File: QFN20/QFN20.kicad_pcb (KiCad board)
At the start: 2 copper layers, 12.2 x 25.7 mm, 10 parts, among them J1 Conn_01x10, J2 Conn_02x10_Counter_Clockwise, J3 Conn_01x10, J4 Conn_02x10_Counter_Clockwise

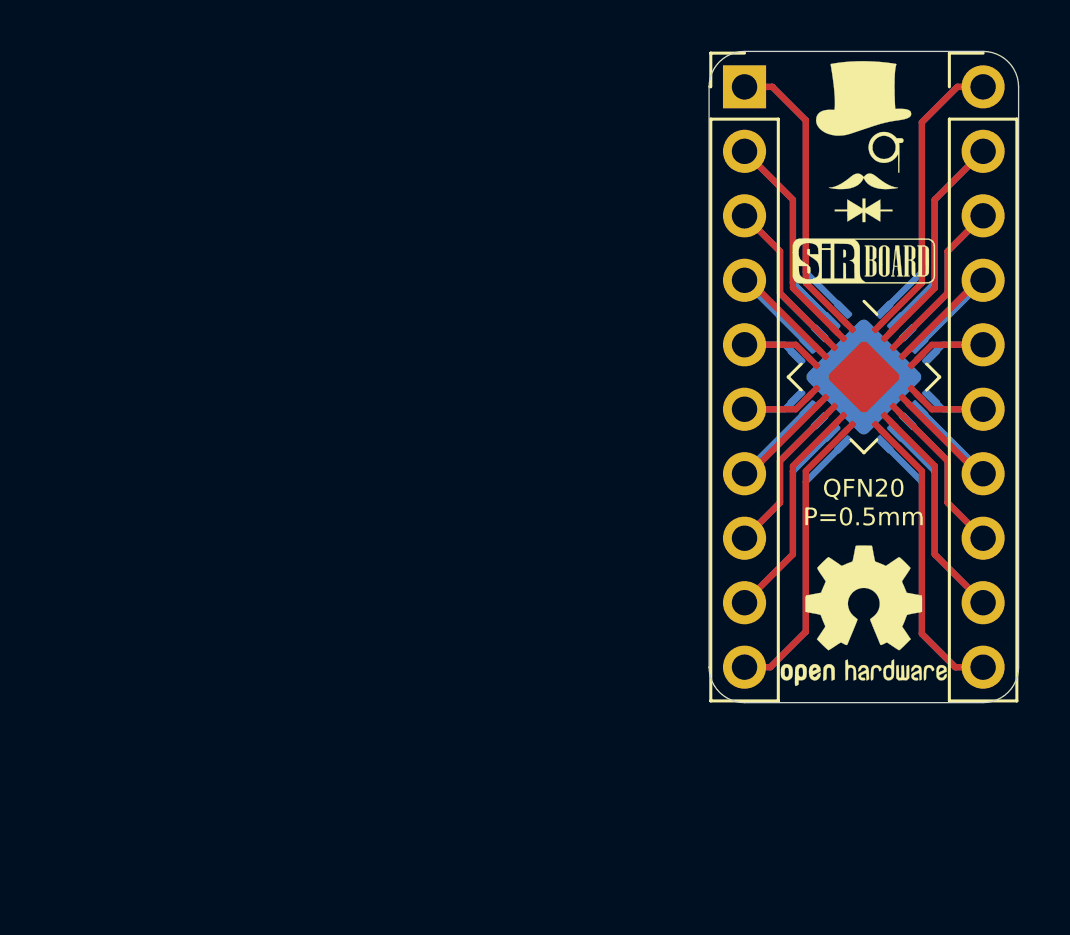
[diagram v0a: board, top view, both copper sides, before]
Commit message: Silkscreens and sizes updated
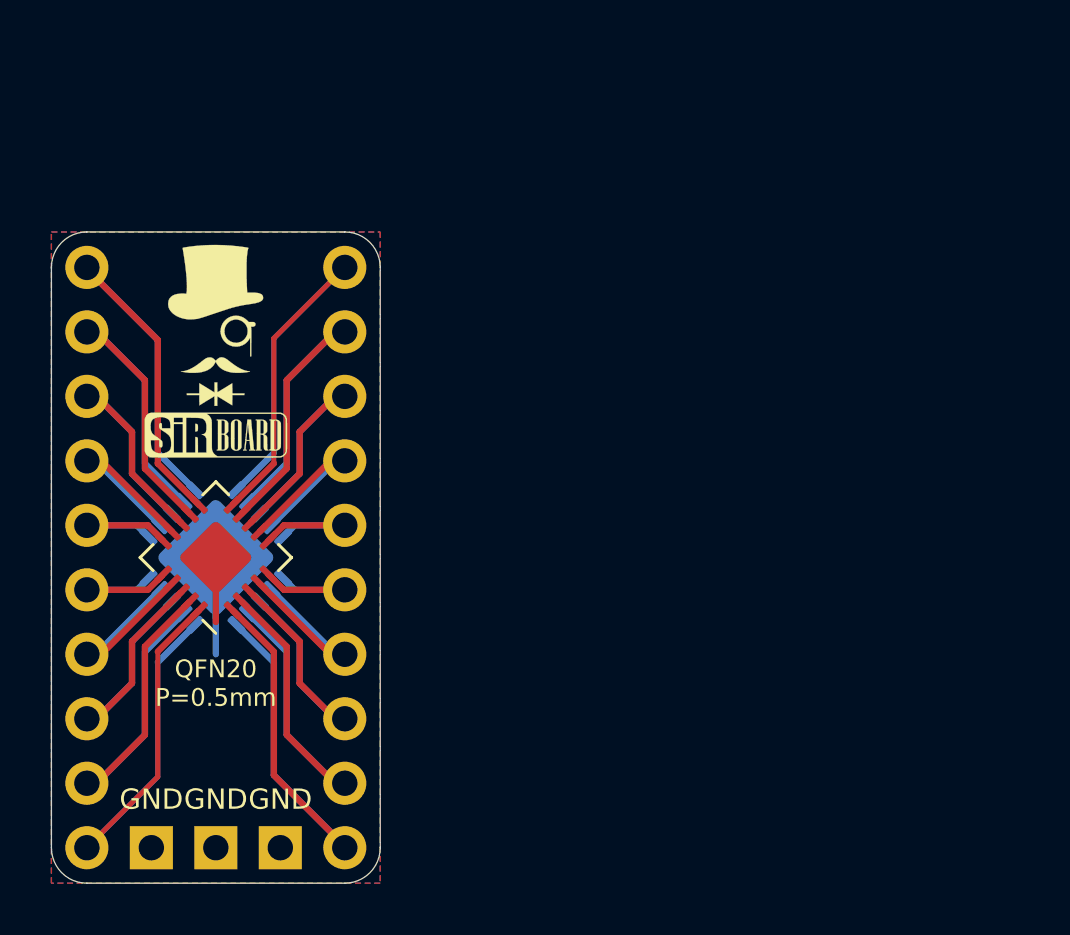
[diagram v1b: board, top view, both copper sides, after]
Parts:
- removed REF** (x2): OSHW-Logo2_7.3x6mm_SilkScreen, Symbol:OSHW-Logo2_7.3x6mm_SilkScreen
- added J5: Conn_01x03, Connector_PinHeader_2.54mm:PinHeader_1x03_P2.54mm_Vertical, F.Cu at (99.3, 70.6)
- moved J3 46.3 mm to (91.7, 70.6), turned to 180 degrees
- moved J1 33.9 mm to (101.9, 70.6), turned to 180 degrees
- moved G*** 27.9 mm to (96.9, 49.9), turned to 180 degrees
- moved G*** 26.5 mm to (96.8, 50.0)
- moved J2 26.5 mm to (96.8, 59.2), turned to 135 degrees
- moved J4 26.5 mm to (96.8, 59.2), turned to 225 degrees
- moved G*** 26.4 mm to (96.8, 54.4)
- moved G*** 25.7 mm to (96.8, 54.4), turned to 180 degrees
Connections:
- J2 pad 21: (no net) -> Net-(J5-Pad1)
- J4 pad 21: (no net) -> Net-(J5-Pad1)
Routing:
- net Net-(J5-Pad1): track 0.00 -> 8.72 mm
- net Net-(J2-Pad11): track 22.7 -> 21.4 mm
- net Net-(J1-Pad1): track 22.7 -> 21.7 mm
- net Net-(J2-Pad20): track 22.6 -> 21.7 mm
- net Net-(J1-Pad10): track 22.6 -> 21.7 mm
- added copper zone on B.Cu, net Net-(J5-Pad1)
- added copper zone on F.Cu, net Net-(J5-Pad1)
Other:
- board size 12.2 x 25.7 mm -> 13 x 25.7 mm
- board text added: "GND"

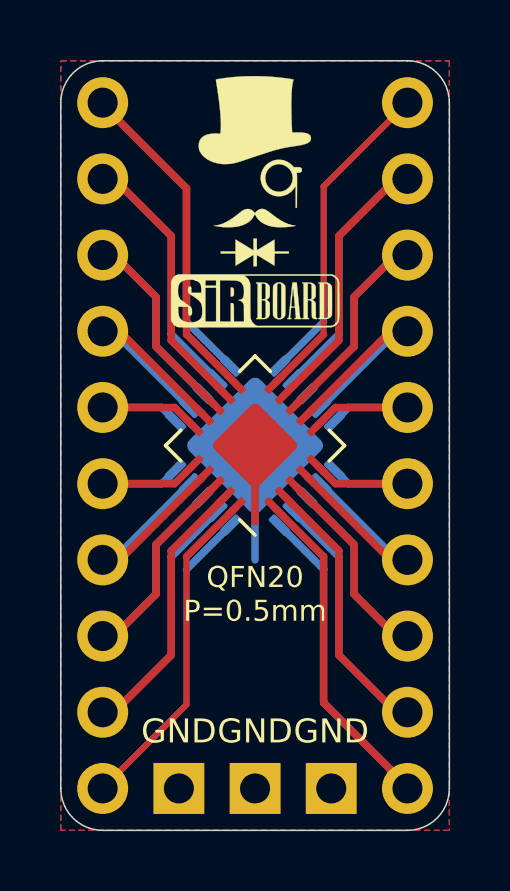
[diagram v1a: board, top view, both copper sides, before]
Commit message: Dimensions Added And TQFP64 Added
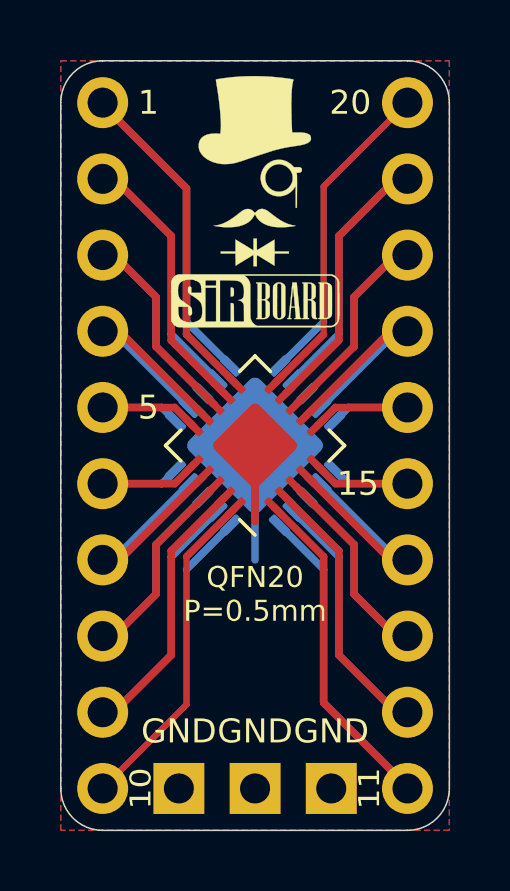
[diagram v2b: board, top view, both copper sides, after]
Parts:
- J1, J3: moved to B.Cu
- turned J1 to 0 degrees
- turned J3 to 0 degrees
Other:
- board text added: "1"
- board text added: "10"
- board text added: "11"
- board text added: "15"
- board text added: "20"
- board text added: "5"

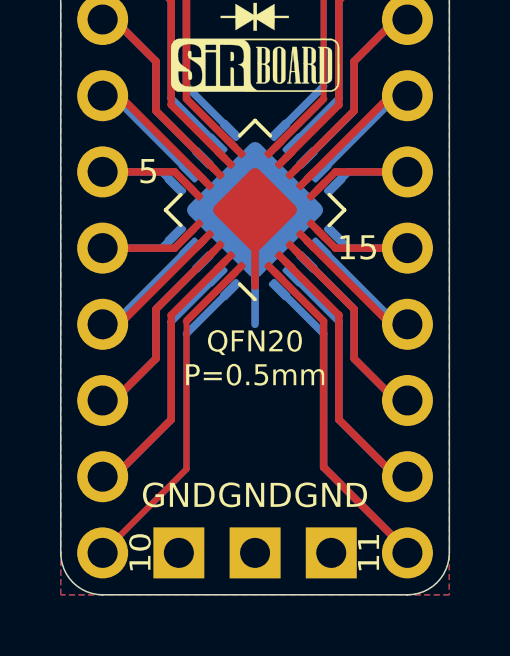
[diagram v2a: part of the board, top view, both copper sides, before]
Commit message: Pin Numbering edited
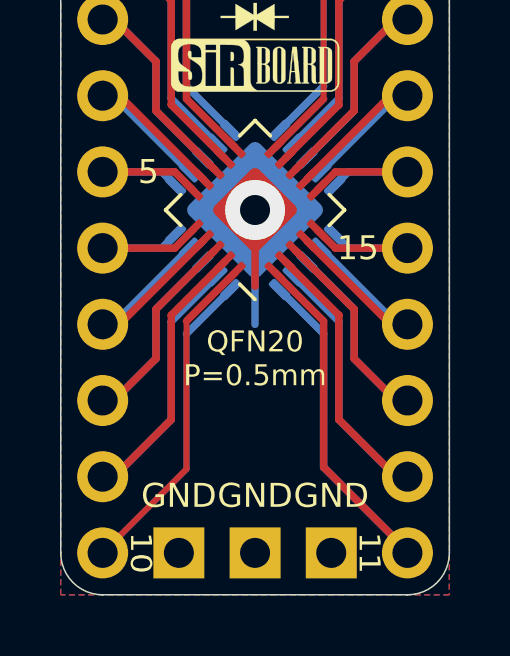
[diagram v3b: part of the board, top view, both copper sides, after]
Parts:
- J1, J3: moved to F.Cu
- J5: moved to B.Cu
- turned J1 to 180 degrees
- turned J3 to 180 degrees
- turned J5 to 90 degrees
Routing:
- net Net-(J5-Pad1): vias 0 -> 1

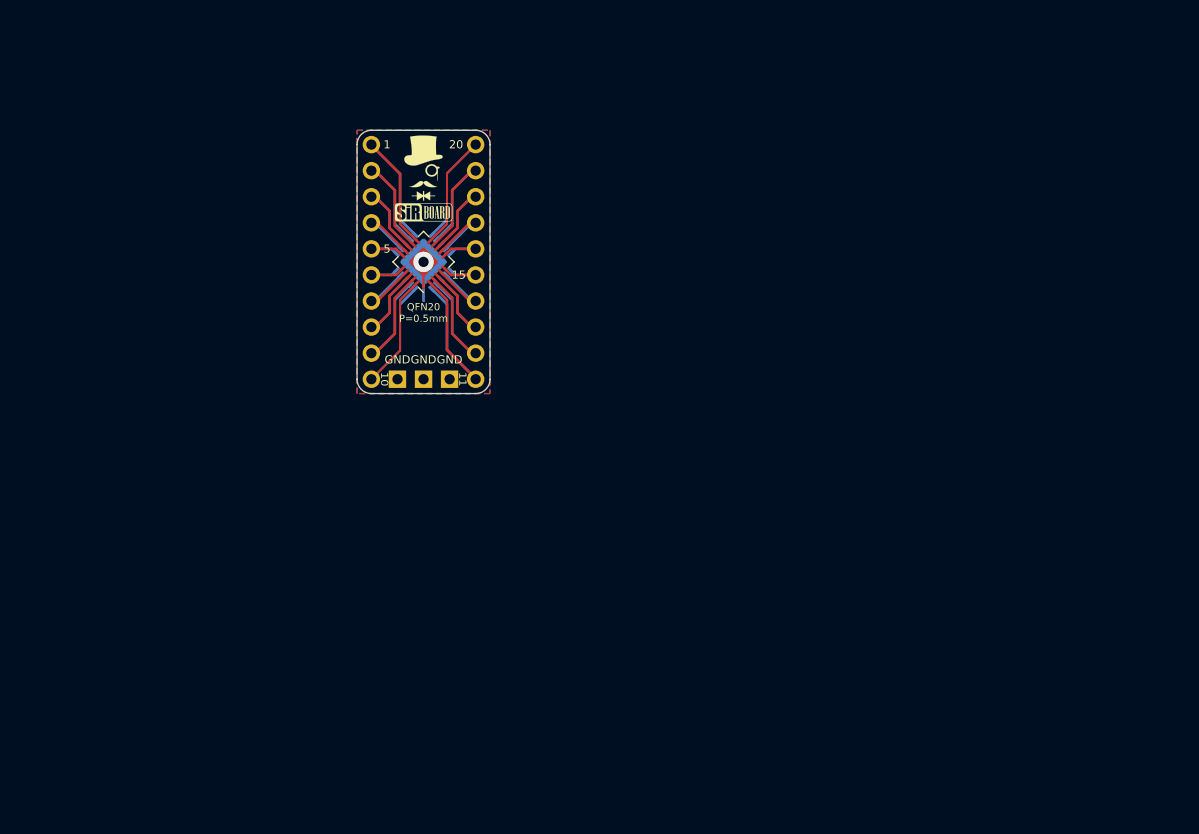
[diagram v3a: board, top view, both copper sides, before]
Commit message: Numbering Orientation Edited
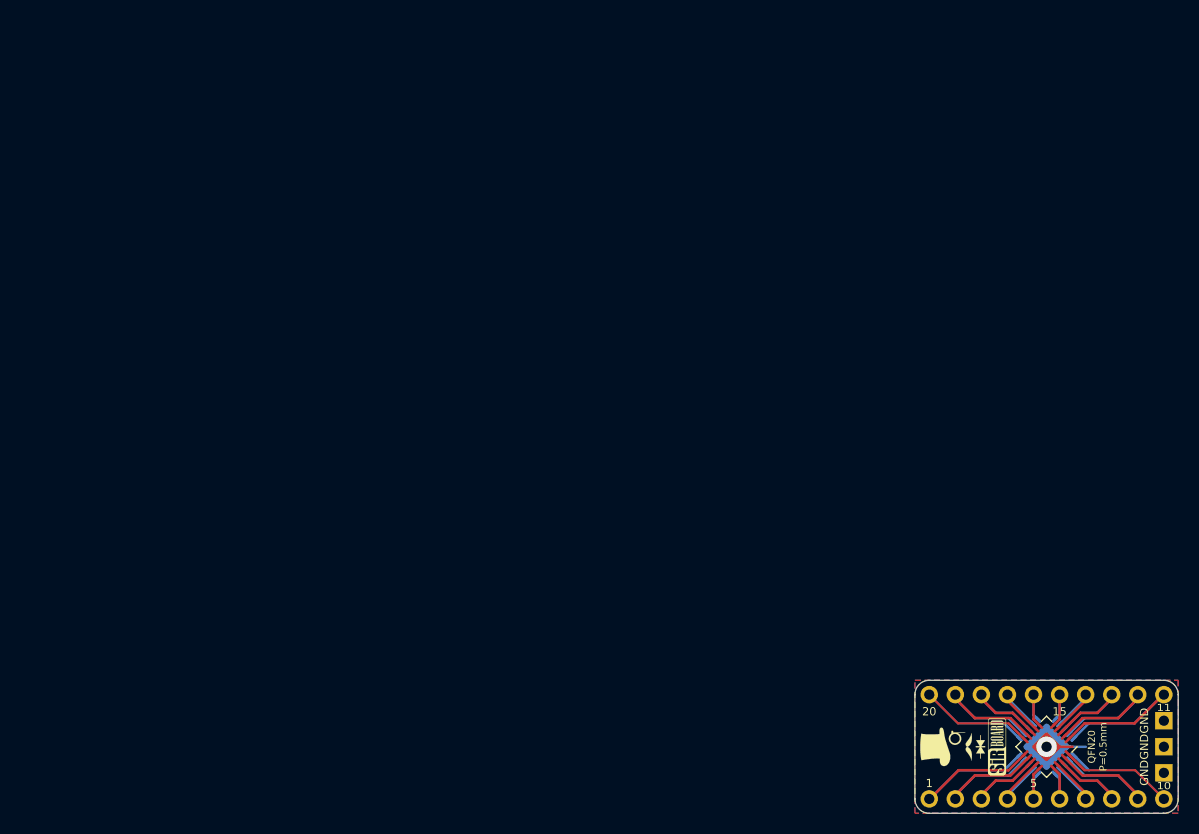
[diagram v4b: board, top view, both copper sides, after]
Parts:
- moved J3 87.4 mm to (168.9, 111.5), turned to 270 degrees
- moved J5 77.1 mm to (168.9, 103.9), turned to 180 degrees
- moved J2 76.9 mm to (157.5, 106.4), turned to 225 degrees
- moved J4 76.9 mm to (157.5, 106.4), turned to 315 degrees
- moved G*** 76.4 mm to (148.3, 106.4), turned to 90 degrees
- moved G*** 76.4 mm to (152.7, 106.4), turned to 270 degrees
- moved G*** 76.4 mm to (152.7, 106.4), turned to 90 degrees
- moved G*** 76.2 mm to (148.2, 106.3), turned to 270 degrees
- moved J1 73.8 mm to (168.9, 101.3), turned to 270 degrees
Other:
- board size 13 x 25.7 mm -> 25.7 x 13 mm

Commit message: Silkscreen Edits
Dimensions moved to Drawings Layer
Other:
- rule pad_to_mask_clearance: 0.051 -> 0
- rule solder_mask_min_width: 0.25 -> 0.1
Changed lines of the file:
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@@
     (pad_size 3.35 3.35)
     (pad_drill 0)
-    (pad_to_mask_clearance 0.051)
-    (solder_mask_min_width 0.25)
+    (pad_to_mask_clearance 0)
+    (solder_mask_min_width 0.1)
     (aux_axis_origin 0 0)
     (visible_elements 7FFFFFFF)
     (pcbplotparams
-      (layerselection 0x010fc_ffffffff)
+      (layerselection 0x010f0_ffffffff)
       (usegerberextensions false)
       (usegerberattributes false)
@@
       (linewidth 0.100000)
       (plotframeref false)
-      (viasonmask false)
+      (viasonmask true)
       (mode 1)
-      (useauxorigin false)
+      (useauxorigin true)
       (hpglpennumber 1)
       (hpglpenspeed 20)
@@
       (psa4output false)
       (plotreference true)
-      (plotvalue true)
+      (plotvalue false)
       (plotinvisibletext false)
       (padsonsilk false)
@@
       (outputformat 1)
       (mirror false)
-      (drillshape 1)
+      (drillshape 0)
       (scaleselection 1)
-      (outputdirectory ""))
+      (outputdirectory "../../Gerbers/QFN20/"))
   )
   (net 0 "")
@@
     )
   )
-  (dimension 22.86 (width 0.15) (layer F.SilkS)
-    (gr_text "22.860 mm" (at 157.48 96.871) (layer F.SilkS)
+  (dimension 22.86 (width 0.15) (layer Dwgs.User)
+    (gr_text "22.860 mm" (at 157.48 96.871) (layer Dwgs.User)
       (effects (font (size 1 1) (thickness 0.15)) hide)
     )
@@
     (arrow2b (pts (xy 146.05 98.171) (xy 147.176504 97.584579)))
   )
-  (dimension 25.654 (width 0.15) (layer F.SilkS)
-    (gr_text "25.654 mm" (at 157.48 94.204) (layer F.SilkS)
+  (dimension 25.654 (width 0.15) (layer Dwgs.User)
+    (gr_text "25.654 mm" (at 157.48 94.204) (layer Dwgs.User)
       (effects (font (size 1 1) (thickness 0.15)) hide)
     )
@@
     (effects (font (size 0.8 0.8) (thickness 0.13)))
   )
-  (dimension 10.16 (width 0.15) (layer F.SilkS)
-    (gr_text "10.160 mm" (at 141.194 106.426 90) (layer F.SilkS)
+  (dimension 10.16 (width 0.15) (layer Dwgs.User)
+    (gr_text "10.160 mm" (at 141.194 106.426 90) (layer Dwgs.User)
       (effects (font (size 1 1) (thickness 0.15)) hide)
     )
@@
     (arrow2b (pts (xy 142.494 111.506) (xy 141.907579 110.379496)))
   )
-  (dimension 12.954 (width 0.15) (layer F.SilkS)
-    (gr_text "12.954 mm" (at 137.892 106.426 90) (layer F.SilkS)
+  (dimension 12.954 (width 0.15) (layer Dwgs.User)
+    (gr_text "12.954 mm" (at 137.892 106.426 90) (layer Dwgs.User)
       (effects (font (size 1 1) (thickness 0.15)) hide)
     )

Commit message: Page Settings Updated
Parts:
- moved G*** 108.3 mm to (61.2, 42.2)
- moved G*** 108.3 mm to (61.1, 42.0)
- moved G*** 108.3 mm to (65.5, 42.2) (x2)
- moved J1 108.3 mm to (81.8, 37.1)
- moved J3 108.3 mm to (81.8, 47.2)
- moved J5 108.3 mm to (81.8, 39.6)
- moved J2 108.3 mm to (70.4, 42.2)
- moved J4 108.3 mm to (70.4, 42.2)

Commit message: Board Updates
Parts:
- moved J1 0.18 mm to (81.9, 37.2)
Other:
- board size 25.7 x 13 mm -> 25.4 x 12.7 mm
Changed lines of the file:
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@@
   )
   (module Connector_PinHeader_2.54mm:PinHeader_1x10_P2.54mm_Vertical (layer F.Cu)
-    (at 81.788 37.084 270)
+    (at 81.915 37.211 270)
     (descr "Through hole straight pin header, 1x10, 2.54mm pitch, single row")
     (tags "Through hole pin header THT 1x10 2.54mm single row")
@@
     )
   )
+  (gr_arc (start 81.788 37.084) (end 83.058 37.084) (angle -90) (layer Edge.Cuts) (width 0.05))
+  (gr_arc (start 81.788 47.244) (end 81.788 48.514) (angle -90) (layer Edge.Cuts) (width 0.05))
+  (gr_arc (start 58.928 47.244) (end 57.658 47.244) (angle -90) (layer Edge.Cuts) (width 0.05))
+  (gr_arc (start 58.928 37.084) (end 58.928 35.814) (angle -90) (layer Edge.Cuts) (width 0.05))
   (dimension 22.86 (width 0.15) (layer Dwgs.User)
     (gr_text "22.860 mm" (at 70.358 32.609) (layer Dwgs.User)
@@
     (arrow2b (pts (xy 58.928 33.909) (xy 60.054504 33.322579)))
   )
-  (dimension 25.654 (width 0.15) (layer Dwgs.User)
-    (gr_text "25.654 mm" (at 70.358 29.942) (layer Dwgs.User)
+  (dimension 25.4 (width 0.15) (layer Dwgs.User)
+    (gr_text "25.400 mm" (at 70.358 30.069) (layer Dwgs.User)
       (effects (font (size 1 1) (thickness 0.15)) hide)
     )
-    (feature1 (pts (xy 83.185 35.687) (xy 83.185 30.655579)))
-    (feature2 (pts (xy 57.531 35.687) (xy 57.531 30.655579)))
-    (crossbar (pts (xy 57.531 31.242) (xy 83.185 31.242)))
-    (arrow1a (pts (xy 83.185 31.242) (xy 82.058496 31.828421)))
-    (arrow1b (pts (xy 83.185 31.242) (xy 82.058496 30.655579)))
-    (arrow2a (pts (xy 57.531 31.242) (xy 58.657504 31.828421)))
-    (arrow2b (pts (xy 57.531 31.242) (xy 58.657504 30.655579)))
+    (feature1 (pts (xy 83.058 37.084) (xy 83.058 30.782579)))
+    (feature2 (pts (xy 57.658 37.084) (xy 57.658 30.782579)))
+    (crossbar (pts (xy 57.658 31.369) (xy 83.058 31.369)))
+    (arrow1a (pts (xy 83.058 31.369) (xy 81.931496 31.955421)))
+    (arrow1b (pts (xy 83.058 31.369) (xy 81.931496 30.782579)))
+    (arrow2a (pts (xy 57.658 31.369) (xy 58.784504 31.955421)))
+    (arrow2b (pts (xy 57.658 31.369) (xy 58.784504 30.782579)))
   )
   (gr_text 11 (at 81.788 45.974 180) (layer B.SilkS)
@@
     (arrow2b (pts (xy 55.372 47.244) (xy 54.785579 46.117496)))
   )
-  (dimension 12.954 (width 0.15) (layer Dwgs.User)
-    (gr_text "12.954 mm" (at 50.77 42.164 90) (layer Dwgs.User)
+  (dimension 12.7 (width 0.15) (layer Dwgs.User)
+    (gr_text "12.700 mm" (at 51.278 42.164 90) (layer Dwgs.User)
       (effects (font (size 1 1) (thickness 0.15)) hide)
     )
-    (feature1 (pts (xy 57.531 35.687) (xy 51.483579 35.687)))
-    (feature2 (pts (xy 57.531 48.641) (xy 51.483579 48.641)))
-    (crossbar (pts (xy 52.07 48.641) (xy 52.07 35.687)))
-    (arrow1a (pts (xy 52.07 35.687) (xy 52.656421 36.813504)))
-    (arrow1b (pts (xy 52.07 35.687) (xy 51.483579 36.813504)))
-    (arrow2a (pts (xy 52.07 48.641) (xy 52.656421 47.514496)))
-    (arrow2b (pts (xy 52.07 48.641) (xy 51.483579 47.514496)))
+    (feature1 (pts (xy 58.928 35.814) (xy 51.991579 35.814)))
+    (feature2 (pts (xy 58.928 48.514) (xy 51.991579 48.514)))
+    (crossbar (pts (xy 52.578 48.514) (xy 52.578 35.814)))
+    (arrow1a (pts (xy 52.578 35.814) (xy 53.164421 36.940504)))
+    (arrow1b (pts (xy 52.578 35.814) (xy 51.991579 36.940504)))
+    (arrow2a (pts (xy 52.578 48.514) (xy 53.164421 47.387496)))
+    (arrow2b (pts (xy 52.578 48.514) (xy 51.991579 47.387496)))
   )
   (gr_text GND (at 79.883 44.704 90) (layer B.SilkS)
@@
     (effects (font (size 0.7 0.7) (thickness 0.15)))
   )
-  (gr_line (start 57.531 37.084) (end 57.531 47.244) (layer Edge.Cuts) (width 0.05))
-  (gr_line (start 81.788 35.687) (end 58.928 35.687) (layer Edge.Cuts) (width 0.05))
-  (gr_line (start 83.185 47.244) (end 83.185 37.084) (layer Edge.Cuts) (width 0.05))
-  (gr_line (start 58.928 48.641) (end 81.788 48.641) (layer Edge.Cuts) (width 0.05))
-  (gr_arc (start 58.928 47.244) (end 57.531 47.244) (angle -90) (layer Edge.Cuts) (width 0.05))
-  (gr_arc (start 58.928 37.084) (end 58.928 35.687) (angle -90) (layer Edge.Cuts) (width 0.05))
-  (gr_arc (start 81.788 37.084) (end 83.185 37.084) (angle -90) (layer Edge.Cuts) (width 0.05))
-  (gr_arc (start 81.788 47.244) (end 81.788 48.641) (angle -90) (layer Edge.Cuts) (width 0.05))
+  (gr_line (start 57.658 37.084) (end 57.658 47.244) (layer Edge.Cuts) (width 0.05))
+  (gr_line (start 81.788 35.814) (end 58.928 35.814) (layer Edge.Cuts) (width 0.05))
+  (gr_line (start 83.058 47.244) (end 83.058 37.084) (layer Edge.Cuts) (width 0.05))
+  (gr_line (start 58.928 48.514) (end 81.788 48.514) (layer Edge.Cuts) (width 0.05))
   (segment (start 68.280874 41.506204) (end 66.65267 39.878) (width 0.25) (layer F.Cu) (net 1))
   (segment (start 67.70635 41.350827) (end 66.233523 39.878) (width 0.25) (layer B.Cu) (net 1))
@@
     (polygon
       (pts
-        (xy 57.531 48.641) (xy 57.531 35.687) (xy 83.185 35.687) (xy 83.185 48.641)
+        (xy 57.658 48.514) (xy 57.658 35.814) (xy 83.058 35.814) (xy 83.058 48.514)
       )
     )
@@
     (polygon
       (pts
-        (xy 57.531 48.641) (xy 57.531 35.687) (xy 83.185 35.687) (xy 83.185 48.641)
+        (xy 57.658 48.514) (xy 57.658 35.814) (xy 83.058 35.814) (xy 83.058 48.514)
       )
     )
